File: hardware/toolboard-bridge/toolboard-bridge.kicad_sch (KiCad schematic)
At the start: 47 parts, among them J1 USB-C 16P, J2 MF3 2x04P, J3 1x2P, J4 2P 9.5mm, J5 1x3P, K1 12V SRD-C, Q1 2N7002, Q2 2N7002, Q3 MMBT3904, U1 TPS54335A, U2 LTV-357T, U4 USBLC6-2SC6

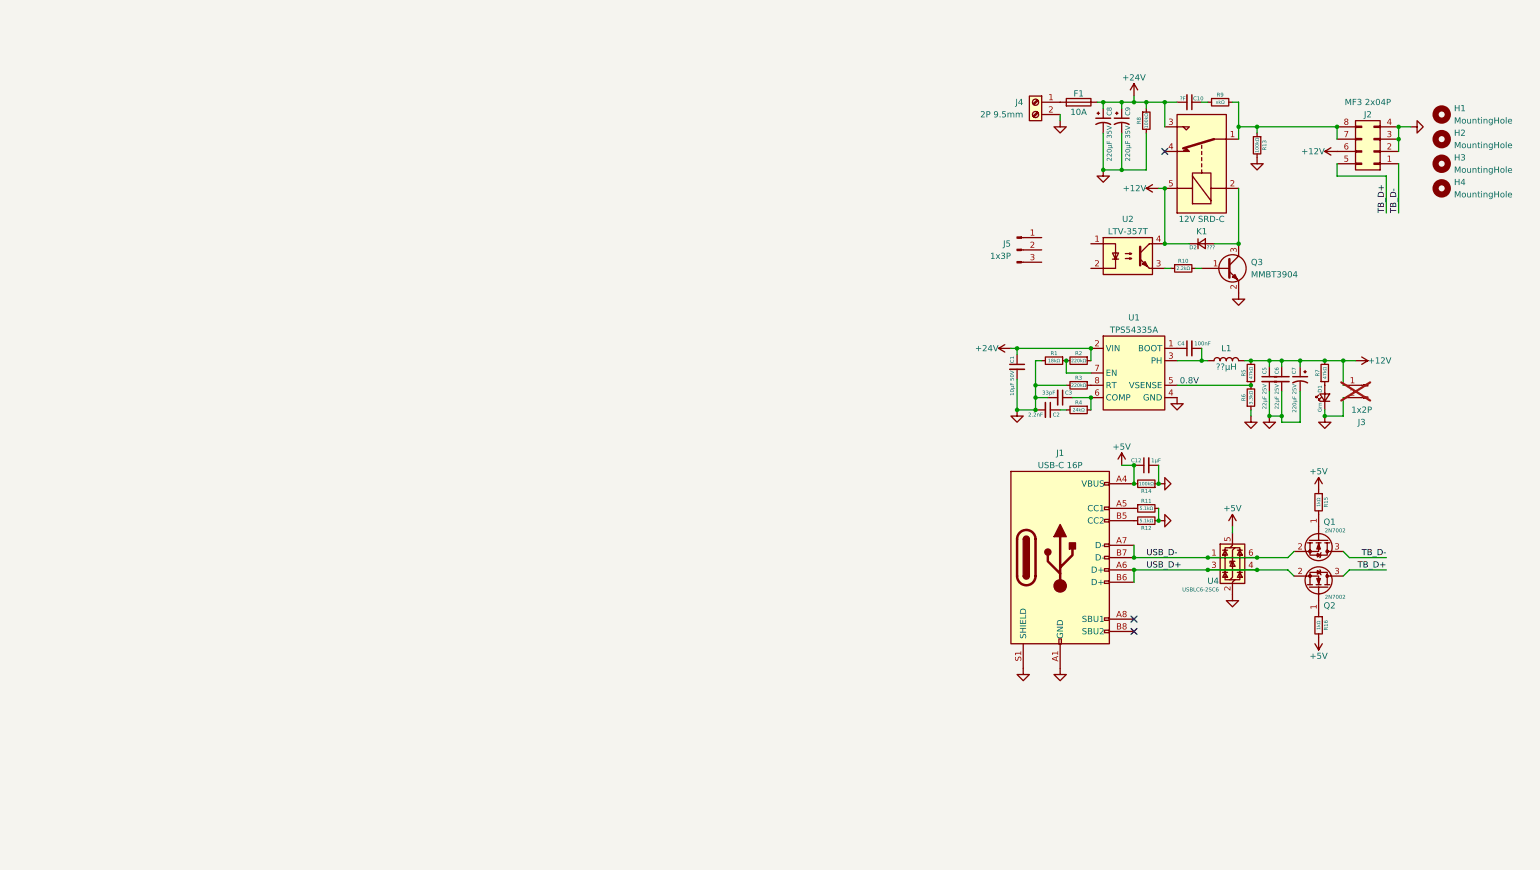
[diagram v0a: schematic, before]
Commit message: cleaned up corevus toolboard schematics to be more presentable
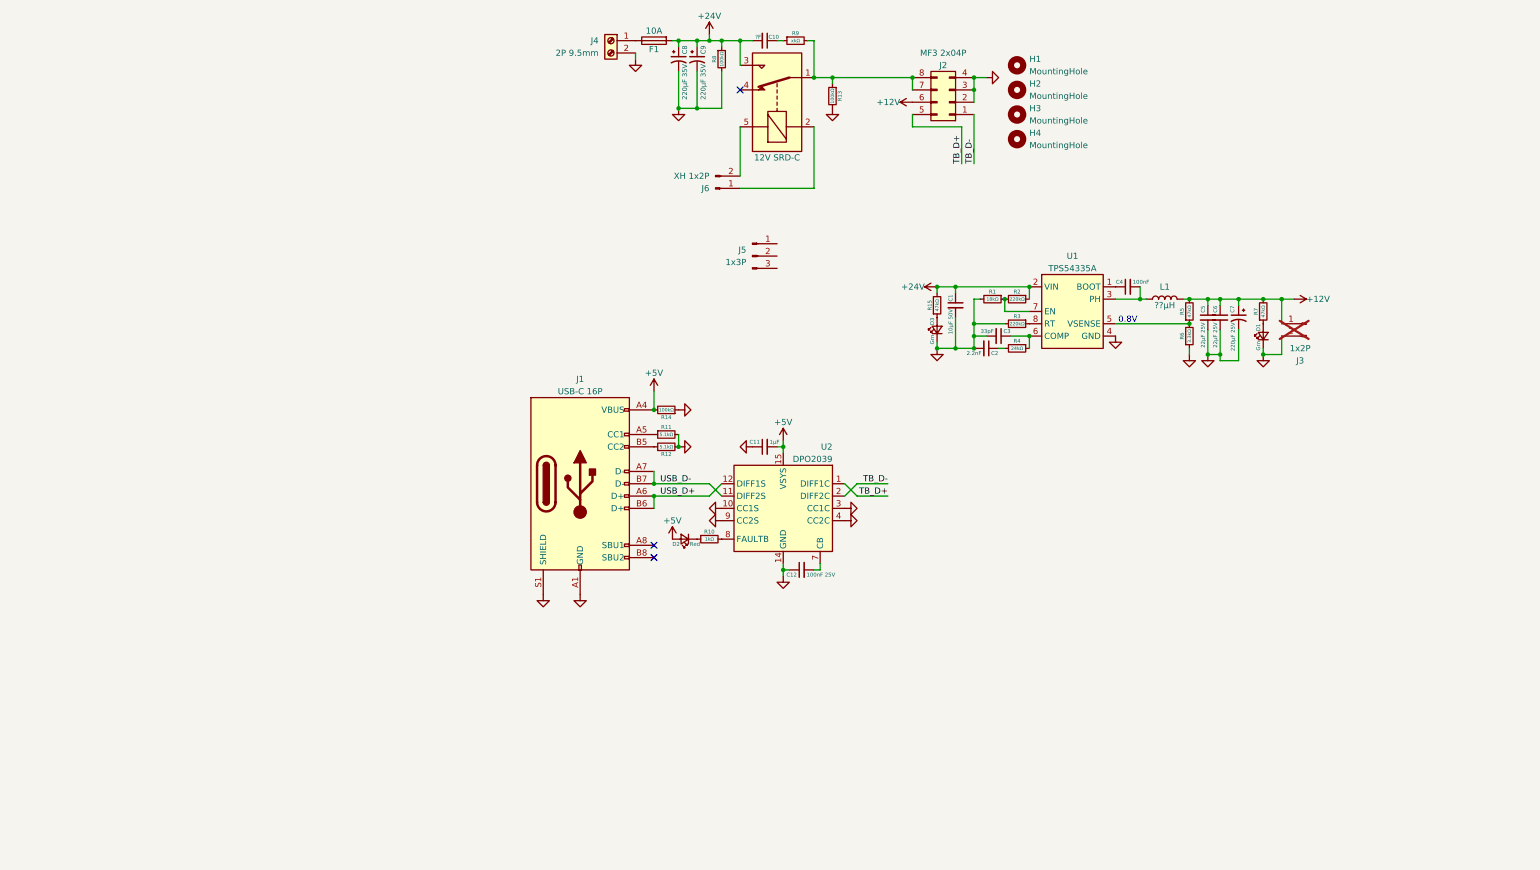
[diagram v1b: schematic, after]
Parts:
- removed D2: ???, Diode_SMD:D_SOD-123, symbol Device:D_Small
- removed Q1, Q2: 2N7002, Package_TO_SOT_SMD:SOT-23, symbol Transistor_FET:2N7002
- removed Q3: MMBT3904, Package_TO_SOT_SMD:SOT-23, symbol Transistor_BJT:MMBT3904
- removed R16: 1kΩ, PCM_ME_passives:0402R, symbol Device:R_Small
- removed U2: LTV-357T, Package_SO:SO-4_4.4x3.6mm_P2.54mm, symbol Isolator:LTV-357T
- removed U4: USBLC6-2SC6, Package_TO_SOT_SMD:SOT-23-6, symbol Power_Protection:USBLC6-2SC6
- added C11: 1μF, PCM_ME_passives:0402C, symbol Device:C_Small
- added D2: Red, PCM_ME_passives:0603LED, symbol Device:LED_Small
- added D3: Grn, PCM_ME_passives:0603LED, symbol Device:LED_Small
- added J6: XH 1x2P, corevus:JST_XH_1x02, symbol Connector:Conn_01x02_Pin
- added U2: DPO2039, Package_DFN_QFN:VQFN-16-1EP_3x3mm_P0.5mm_EP1.6x1.6mm, symbol corevus:DPO2039
- C12: value 1μF -> 100nF 25V
- R10: value 2.2kΩ -> 1kΩ
- R15: value 1kΩ -> 47kΩ
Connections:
- net +12V: no longer K1.5
- net +24V: now also F1.2, R15.2; no longer F1.1
- net +5V: now also C11.2, D2.2 (A), U2.15 (VSYS); no longer C12.1, R15.1
- net GND: now also C12.1, C11.1, D3.1 (K), U2.10 (CC1S), U2.13 (NC), U2.14 (GND), U2.16 (NC), U2.17 (GND), U2.3 (CC1C), U2.4 (CC2C), U2.5 (NC), U2.6 (NC), U2.9 (CC2S); no longer C12.2
- net TB_D+: now also U2.1 (DIFF1C)
- net TB_D-: now also U2.2 (DIFF2C)
- net USB_D+: now also U2.12 (DIFF1S)
- net USB_D-: now also U2.11 (DIFF2S)
- net at J4.1 (Pin_1): now also F1.1; no longer F1.2
- net at R10.1: now also D2.1 (K)
- net at R10.2: now also U2.8 (FAULTB)
- net at K1.2: now also J6.1 (Pin_1)
- new net: J6.2 (Pin_2), K1.5
- new net: D3.2 (A), R15.1
- new net: C12.2, U2.7 (CB)
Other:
- company: (none) -> Meridi Engineering
- title: (none) -> Corevus Toolboard Bridge
- moved on the sheet: C1, C10, C2, C3, C4, C5, C6, C7, C8, C9, D1, F1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

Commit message: Added STEP and Parasolid mechanical files for Corevus-G v0.6, added TMC2160 + Heater module, added toolboard 4x thermistor expansion, added toolboard MAX31856 thermocouple ADC expansion
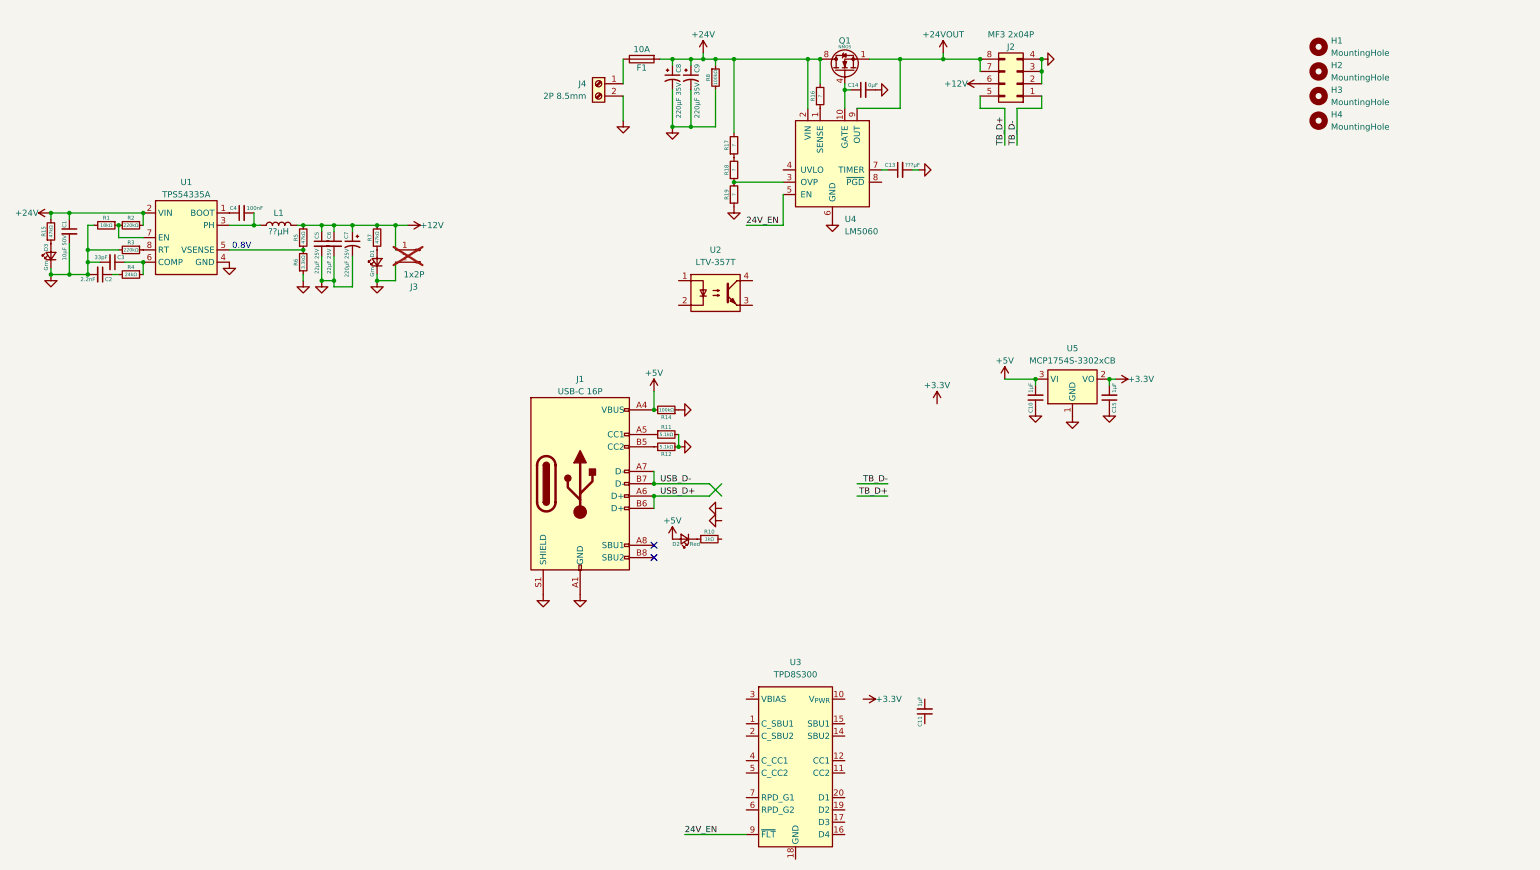
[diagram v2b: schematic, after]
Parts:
- removed C12: 100nF 25V, PCM_ME_passives:0402C, symbol Device:C_Small
- removed J5: 1x3P, corevus:PinHeader_1x03_P2.54mm_Vertical, symbol Connector:Conn_01x03_Pin
- removed J6: XH 1x2P, corevus:JST_XH_1x02, symbol Connector:Conn_01x02_Pin
- removed K1: 12V SRD-C, Relay_THT:Relay_SPDT_SANYOU_SRD_Series_Form_C, symbol Relay:SANYOU_SRD_Form_C
- removed R13: 100kΩ, PCM_ME_passives:0402R, symbol Device:R_Small
- removed R9: xkΩ, PCM_ME_passives:0402R, symbol Device:R_Small
- removed U2: DPO2039, Package_DFN_QFN:VQFN-16-1EP_3x3mm_P0.5mm_EP1.6x1.6mm, symbol corevus:DPO2039
- added C13: ???μF, PCM_ME_passives:0402C, symbol Device:C_Small
- added C14: 0μF, PCM_ME_passives:0603C, symbol Device:C_Small
- added C15: 1μF, PCM_ME_passives:0402C, symbol Device:C_Small
- added Q1: NMOS, corevus:MOSFET_DFN8_5x6, symbol corevus:NMOS_DFN8
- added R16: ?, PCM_ME_passives:0402R, symbol Device:R_Small
- added R17, R18, R19: ?, PCM_ME_passives:0603R, symbol Device:R_Small
- added U2: LTV-357T, Package_SO:SO-4_4.4x3.6mm_P2.54mm, symbol Isolator:LTV-357T
- added U3: TPD8S300, Package_DFN_QFN:WQFN-20-1EP_3x3mm_P0.4mm_EP1.7x1.7mm, symbol corevus:TPD8S300
- added U4: LM5060, Package_SO:MSOP-10_3x3mm_P0.5mm, symbol Power_Management:LM5060
- added U5: MCP1754S-3302xCB, Package_TO_SOT_SMD:SOT-23, symbol Regulator_Linear:MCP1754S-3302xCB
- C10: value ?F -> 1μF; footprint Capacitor_SMD:C_1206_3216Metric -> PCM_ME_passives:0402C
- J4: value 2P 9.5mm -> 2P 8.5mm
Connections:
- net +24V: now also Q1.5 (D), Q1.6 (D), Q1.7 (D), Q1.8 (D), R16.2, R17.2, U4.2 (VIN); no longer C10.2
- net +5V: now also C10.2, U5.3 (VI); no longer C11.2
- net GND: now also C10.1, C13.2, C14.2, C15.1, R19.1, U4.6 (GND), U5.1 (GND); no longer C11.1
- net +24VOUT: now reaches J2.7 (Pin_7), J2.8 (Pin_8)
- net +24VOUT: now also Q1.1 (S), Q1.2 (S), Q1.3 (S), U4.9 (OUT)
- new net: R18.1, R19.2, U4.3 (OVP)
- new net: U3.13 (GND), U3.18 (GND), U3.21 (GND), U3.8 (GND)
- new net: C13.1, U4.7 (TIMER)
- new net: R16.1, U4.1 (SENSE)
- new net: R17.1, R18.2
- new net: C14.1, Q1.4 (G), U4.10 (GATE)
- new net +3.3V: C15.2, U5.2 (VO)
- new net 24V_EN: U3.9 (~{FLT}), U4.5 (EN)
- no-connect marks 3 -> 2
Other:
- moved on the sheet: C1, C2, C3, C4, C5, C6, C7, C8, C9, D1, D3, F1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
